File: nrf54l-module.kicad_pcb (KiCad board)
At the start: 4 copper layers, 16 x 25 mm, 127 parts, among them SW1 TS24CA, U1 NRF54L15-QFAA-R, U2 XL-0201SURC, U3 TLV62569DBVR, U4 XL-0201SURC, U5 XL-0201SURC, X1 XL7EL89CKI-111YLC-32M

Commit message: chore: refactoring
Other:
- board text removed: "RESET"
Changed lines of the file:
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@@
-		)
-	)
-	(gr_text "RESET"
-		(at 27.152888 32.092612 90)
-		(layer "B.SilkS")
-		(effects
-			(font
-				(face "Comfortaa")
-				(size 0.92 0.92)
-				(thickness 0.175)
-			)
-			(justify left bottom mirror)
-		)
-		(render_cache "RESET" 90
-			(polygon
-				(pts
-					(xy 26.966447 32.224932) (xy 26.982331 32.235467) (xy 26.992865 32.251351) (xy 26.996488 32.271532)
-					(xy 26.992868 32.291664) (xy 26.982331 32.30754) (xy 26.966447 32.318075) (xy 26.946266 32.321697)
-					(xy 26.602639 32.321697) (xy 26.602639 32.512189) (xy 26.601347 32.534098) (xy 26.970759 32.765767)
-					(xy 26.990083 32.783125) (xy 26.994729 32.793927) (xy 26.996488 32.809528) (xy 26.993573 32.831362)
-					(xy 26.985773 32.846392) (xy 26.973343 32.856491) (xy 26.957874 32.861081) (xy 26.940331 32.859188)
-					(xy 26.919246 32.849413) (xy 26.58073 32.63836) (xy 26.555079 32.694935) (xy 26.520313 32.742607)
-					(xy 26.475906 32.782507) (xy 26.424256 32.812252) (xy 26.366627 32.830315) (xy 26.30148 32.836548)
-					(xy 26.241714 32.831699) (xy 26.188233 32.81765) (xy 26.139918 32.794697) (xy 26.096596 32.763339)
-					(xy 26.060311 32.725178) (xy 26.030544 32.679537) (xy 26.009042 32.629291) (xy 25.995837 32.573848)
-					(xy 25.991277 32.512189) (xy 26.087787 32.512189) (xy 26.090935 32.55529) (xy 26.100032 32.593884)
-					(xy 26.114807 32.628698) (xy 26.135305 32.660382) (xy 26.160299 32.687047) (xy 26.190139 32.709142)
-					(xy 26.223419 32.725388) (xy 26.260268 32.735319) (xy 26.30148 32.738746) (xy 26.340041 32.735357)
-					(xy 26.374966 32.725468) (xy 26.406978 32.709142) (xy 26.435547 32.687149) (xy 26.459706 32.660499)
-					(xy 26.479726 32.628698) (xy 26.494152 32.593918) (xy 26.503048 32.555321) (xy 26.506128 32.512189)
-					(xy 26.506128 32.321697) (xy 26.087787 32.321697) (xy 26.087787 32.512189) (xy 25.991277 32.512189)
-					(xy 25.991277 32.271532) (xy 25.994899 32.251351) (xy 26.005433 32.235467) (xy 26.02131 32.22493)
-					(xy 26.041442 32.22131) (xy 26.946266 32.22131)
-				)
-			)
-			(polygon
-				(pts
-					(xy 26.996488 33.066982) (xy 26.992865 33.046801) (xy 26.982331 33.030917) (xy 26.966447 33.020383)
-					(xy 26.946266 33.01676) (xy 26.041442 33.01676) (xy 26.02131 33.02038) (xy 26.005433 33.030917)
-					(xy 25.994899 33.046801) (xy 25.991277 33.066982) (xy 25.991277 33.670591) (xy 25.994686 33.689811)
-					(xy 26.004815 33.705982) (xy 26.020191 33.717021) (xy 26.04015 33.720812) (xy 26.058054 33.717162)
-					(xy 26.073631 33.705982) (xy 26.084241 33.689764) (xy 26.087787 33.670591) (xy 26.087787 33.117147)
-					(xy 26.443043 33.117147) (xy 26.443043 33.52004) (xy 26.446663 33.540172) (xy 26.457199 33.556049)
-					(xy 26.472897 33.566642) (xy 26.491916 33.570205) (xy 26.510983 33.566639) (xy 26.526689 33.556049)
-					(xy 26.537225 33.540172) (xy 26.540845 33.52004) (xy 26.540845 33.117147) (xy 26.899977 33.117147)
-					(xy 26.899977 33.670591) (xy 26.903523 33.689764) (xy 26.914134 33.705982) (xy 26.929703 33.717164)
-					(xy 26.947558 33.720812) (xy 26.967576 33.71702) (xy 26.983005 33.705982) (xy 26.993091 33.689816)
-					(xy 26.996488 33.670591)
-				)
-			)
-			(polygon
-				(pts
-					(xy 27.009352 34.216396) (xy 27.003205 34.135423) (xy 26.985453 34.063179) (xy 26.956603 33.998209)
-					(xy 26.916523 33.940019) (xy 26.869941 33.895765) (xy 26.816275 33.863724) (xy 26.796142 33.858425)
-					(xy 26.778357 33.863106) (xy 26.763987 33.87574) (xy 26.754538 33.895913) (xy 26.752913 33.91368)
-					(xy 26.758414 33.931303) (xy 26.7696 33.946535) (xy 26.785379 33.957706) (xy 26.819936 33.980934)
-					(xy 26.850784 34.013043) (xy 26.878125 34.055508) (xy 26.89767 34.102244) (xy 26.909864 34.155468)
-					(xy 26.914134 34.216396) (xy 26.908192 34.282572) (xy 26.891423 34.337853) (xy 26.864587 34.384362)
-					(xy 26.837354 34.413084) (xy 26.80511 34.433514) (xy 26.766858 34.446177) (xy 26.721057 34.450649)
-					(xy 26.671107 34.444206) (xy 26.626562 34.425197) (xy 26.585898 34.392732) (xy 26.561977 34.362535)
-					(xy 26.54165 34.323505) (xy 26.525327 34.273808) (xy 26.513825 34.211228) (xy 26.500219 34.135924)
-					(xy 26.47972 34.072692) (xy 26.45305 34.019763) (xy 26.420516 33.975682) (xy 26.379972 33.937937)
-					(xy 26.336262 33.911777) (xy 26.288604 33.896098) (xy 26.23581 33.890744) (xy 26.18482 33.895577)
-					(xy 26.139735 33.909572) (xy 26.099359 33.932595) (xy 26.064197 33.96345) (xy 26.034438 34.001522)
-					(xy 26.009927 34.047812) (xy 25.992811 34.097656) (xy 25.982134 34.153533) (xy 25.978412 34.216396)
-					(xy 25.984122 34.286236) (xy 26.000418 34.346587) (xy 26.026668 34.399136) (xy 26.061729 34.447046)
-					(xy 26.099659 34.485774) (xy 26.140592 34.516319) (xy 26.161364 34.524935) (xy 26.180477 34.524633)
-					(xy 26.197422 34.516837) (xy 26.210082 34.502162) (xy 26.215225 34.48264) (xy 26.212666 34.462896)
-					(xy 26.203299 34.445338) (xy 26.188173 34.432617) (xy 26.146481 34.398334) (xy 26.109021 34.352173)
-					(xy 26.090812 34.316678) (xy 26.078662 34.27175) (xy 26.073631 34.215104) (xy 26.078967 34.148515)
-					(xy 26.093735 34.09487) (xy 26.116774 34.051632) (xy 26.140692 34.024695) (xy 26.168929 34.005707)
-					(xy 26.202329 33.994012) (xy 26.24227 33.989895) (xy 26.283734 33.995699) (xy 26.321484 34.013059)
-					(xy 26.356813 34.043262) (xy 26.383179 34.082207) (xy 26.406497 34.142942) (xy 26.425011 34.233136)
-					(xy 26.441429 34.314395) (xy 26.463868 34.379582) (xy 26.491378 34.431344) (xy 26.523487 34.471884)
-					(xy 26.563494 34.505617) (xy 26.608783 34.529714) (xy 26.660392 34.544565) (xy 26.719765 34.549743)
-					(xy 26.780191 34.544498) (xy 26.832233 34.529516) (xy 26.877451 34.505308) (xy 26.917063 34.472433)
-					(xy 26.949765 34.43261) (xy 26.975927 34.38498) (xy 26.994248 34.333423) (xy 27.005489 34.277474)
-				)
-			)
-			(polygon
-				(pts
-					(xy 26.996488 34.809781) (xy 26.992865 34.789601) (xy 26.982331 34.773717) (xy 26.966447 34.763182)
-					(xy 26.946266 34.75956) (xy 26.041442 34.75956) (xy 26.02131 34.76318) (xy 26.005433 34.773717)
-					(xy 25.994899 34.789601) (xy 25.991277 34.809781) (xy 25.991277 35.413391) (xy 25.994686 35.432611)
-					(xy 26.004815 35.448782) (xy 26.020191 35.45982) (xy 26.04015 35.463612) (xy 26.058054 35.459961)
-					(xy 26.073631 35.448782) (xy 26.084241 35.432564) (xy 26.087787 35.413391) (xy 26.087787 34.859946)
-					(xy 26.443043 34.859946) (xy 26.443043 35.26284) (xy 26.446663 35.282972) (xy 26.457199 35.298848)
-					(xy 26.472897 35.309441) (xy 26.491916 35.313005) (xy 26.510983 35.309439) (xy 26.526689 35.298848)
-					(xy 26.537225 35.282972) (xy 26.540845 35.26284) (xy 26.540845 34.859946) (xy 26.899977 34.859946)
-					(xy 26.899977 35.413391) (xy 26.903523 35.432564) (xy 26.914134 35.448782) (xy 26.929703 35.459964)
-					(xy 26.947558 35.463612) (xy 26.967576 35.45982) (xy 26.983005 35.448782) (xy 26.993091 35.432615)
-					(xy 26.996488 35.413391)
-				)
-			)
-			(polygon
-				(pts
-					(xy 26.996488 35.942455) (xy 26.992811 35.923368) (xy 26.981713 35.907064) (xy 26.965401 35.895969)
-					(xy 26.946266 35.89229) (xy 26.082619 35.89229) (xy 26.082619 35.587255) (xy 26.079298 35.568306)
-					(xy 26.069754 35.553774) (xy 26.055408 35.544174) (xy 26.037622 35.54091) (xy 26.018673 35.544231)
-					(xy 26.004141 35.553774) (xy 25.994598 35.568306) (xy 25.991277 35.587255) (xy 25.991277 36.299003)
-					(xy 25.994596 36.317904) (xy 26.004141 36.332428) (xy 26.018677 36.342015) (xy 26.037622 36.345348)
-					(xy 26.055404 36.342072) (xy 26.069754 36.332428) (xy 26.0793 36.317904) (xy 26.082619 36.299003)
-					(xy 26.082619 35.992676) (xy 26.946266 35.992676) (xy 26.965449 35.989132) (xy 26.981713 35.97852)
-					(xy 26.992728 35.962585)
-				)
-			)
 		)
 	)

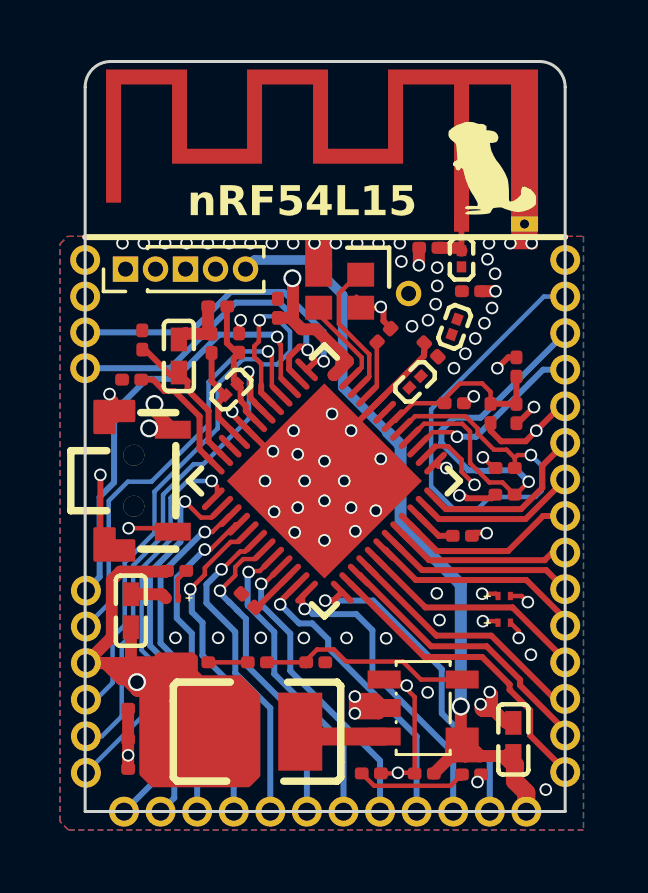
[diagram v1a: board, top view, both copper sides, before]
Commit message: feat: 1.27 mm pitch
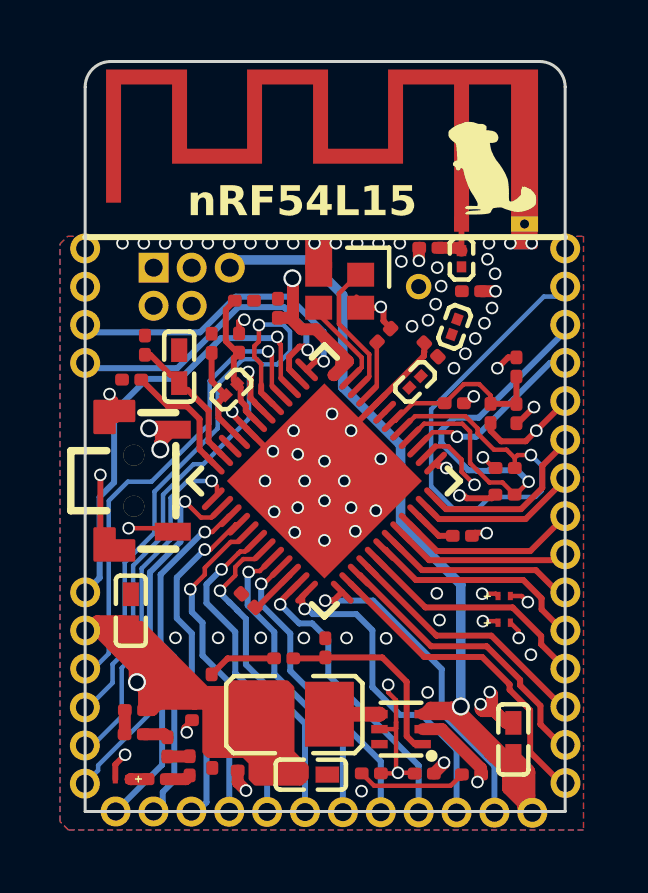
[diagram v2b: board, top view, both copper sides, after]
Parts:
- removed the ? at (25.8, 41.5)
- removed the ? at (32.0, 45.3)
- removed the ? at (25.8, 30.5)
- removed the ? at (40.5, 45.3)
- removed the ? at (39.3, 45.3)
- removed the ? at (41.8, 36.6)
- removed the ? at (25.8, 44.0)
- removed the ? at (41.8, 37.8)
- removed the ? at (41.8, 35.4)
- removed the ? at (41.8, 29.3)
- removed the ? at (41.8, 39.1)
- removed the ? at (41.8, 31.7)
- removed the ? at (30.8, 45.3)
- removed the ? at (41.8, 40.3)
- removed the ? at (41.8, 28.1)
- removed the ? at (36.9, 45.3)
- removed the ? at (41.8, 42.7)
- removed the ? at (41.8, 41.5)
- removed the ? at (25.8, 37.9)
- removed the ? at (25.8, 29.3)
- removed the ? at (35.6, 45.3)
- removed the ? at (41.8, 33.0)
- removed the ? at (38.1, 45.3)
- removed the ? at (34.4, 45.3)
- removed the ? at (28.3, 45.3)
- removed the ? at (41.8, 43.9)
- removed the ? at (41.8, 30.5)
- removed the ? at (25.8, 39.1)
- removed the ? at (33.2, 45.3)
- removed the ? at (29.5, 45.3)
- removed the ? at (25.8, 42.7)
- removed the ? at (25.8, 40.3)
- removed the ? at (41.8, 34.2)
- removed the REF** at (27.2, 27.2)
- removed U3: TLV62569DBVR, easyeda2kicad:SOT-23-5_L3.0-W1.7-P0.95-LS2.8-BR
- removed kibuzzard-68448C78: G***, kibuzzard-68448C78
- removed kibuzzard-68448FBA (x2): G***, kibuzzard-68448FBA
- removed kibuzzard-68449008: G***, kibuzzard-68449008
- removed kibuzzard-68449057: G***, kibuzzard-68449057
- removed kibuzzard-684495BB: G***, kibuzzard-684495BB
- removed kibuzzard-6844ABB3: G***, kibuzzard-6844ABB3
- removed kibuzzard-6844ABB6: G***, kibuzzard-6844ABB6
- added ?: , , F.Cu at (25.8, 41.8)
- added ?: , , F.Cu at (31.9, 45.3)
- added ?: , , F.Cu at (41.8, 27.8)
- added ?: , , F.Cu at (41.8, 34.1)
- added ?: , , F.Cu at (41.8, 32.9)
- added ?: , , F.Cu at (41.8, 29.0)
- added ?: , , F.Cu at (41.8, 35.4)
- added ?: , , F.Cu at (41.8, 41.8)
- added ?: , , F.Cu at (25.8, 40.5)
- added ?: , , F.Cu at (41.8, 36.7)
- added ?: , , F.Cu at (41.8, 31.6)
- added ?: , , F.Cu at (28.1, 28.4)
- added ?: , , F.Cu at (33.1, 45.3)
- added ?: , , F.Cu at (41.8, 39.2)
- added ?: , , F.Cu at (28.1, 45.3)
- added ?: , , F.Cu at (25.8, 29.0)
- added ?: , , F.Cu at (41.8, 40.5)
- added ?: , , F.Cu at (25.8, 44.3)
- added ?: , , F.Cu at (29.3, 45.3)
- added ?: , , F.Cu at (40.7, 45.3)
- added ?: , , F.Cu at (25.8, 43.1)
- added ?: , , F.Cu at (29.4, 28.4)
- added ?: , , F.Cu at (29.4, 27.1)
- added ?: , , F.Cu at (34.4, 45.3)
- added ?: , , F.Cu at (30.6, 45.3)
- added ?: , , F.Cu at (25.8, 39.2)
- added ?: , , F.Cu at (28.1, 27.1)
- added ?: , , F.Cu at (41.8, 30.3)
- added ?: , , F.Cu at (38.2, 45.3)
- added ?: , , F.Cu at (39.5, 45.3)
- added ?: , , F.Cu at (41.8, 44.3)
- added ?: , , F.Cu at (36.9, 45.3)
- added ?: , , F.Cu at (25.8, 30.3)
- added ?: , , F.Cu at (41.8, 43.0)
- added ?: , , F.Cu at (30.6, 27.1)
- added ?: , , F.Cu at (35.7, 45.3)
- added ?: , , F.Cu at (25.8, 38.0)
- added ?: , , F.Cu at (41.8, 38.0)
- added C22: 10uF, easyeda2kicad:C0402, F.Cu at (33.3, 44.0)
- added R11: 1kΩ, Resistor_SMD:R_0201_0603Metric, F.Cu at (29.3, 43.7)
- added R12: 1kΩ, Resistor_SMD:R_0201_0603Metric, F.Cu at (28.5, 43.1)
- added R13: 1kΩ, Resistor_SMD:R_0201_0603Metric, F.Cu at (27.4, 42.7)
- added R14: 1kΩ, Resistor_SMD:R_0201_0603Metric, F.Cu at (27.4, 41.9)
- added U6: TLV62569DRLR, easyeda2kicad:SOT-563_L1.6-W1.2-P0.50-LS1.6-BL, F.Cu at (36.3, 42.5)
- added kibuzzard-6846144B: G***, kibuzzard-6846144B, B.Cu at (28.1, 25.5)
- added kibuzzard-68461451: G***, kibuzzard-68461451, B.Cu at (29.3, 25.5)
- added kibuzzard-68461457: G***, kibuzzard-68461457, B.Cu at (30.6, 25.5)
- added kibuzzard-684616DE: G***, kibuzzard-684616DE, B.Cu at (31.2, 29.5)
- added kibuzzard-6846173A: G***, kibuzzard-6846173A, B.Cu at (30.9, 28.4)
- added kibuzzard-68461772: G***, kibuzzard-68461772, B.Cu at (29.1, 22.0)
- added kibuzzard-68461788: G***, kibuzzard-68461788, B.Cu at (34.8, 27.8)
- added kibuzzard-684617E6: G***, kibuzzard-684617E6, B.Cu at (39.9, 44.3)
- added kibuzzard-684617F6: G***, kibuzzard-684617F6, B.Cu at (27.8, 44.3)
- L4: value 2.2uH -> 1uH; footprint easyeda2kicad:IND-SMD_L3.2-W2.5-LQH32CN1R0M53L -> easyeda2kicad:L1008
- moved R2 6.97 mm to (28.2, 44.2), turned to 0 degrees
- moved U2 6.26 mm to (27.0, 44.2)
- moved kibuzzard-68448B88 6.21 mm to (28.5, 23.1)
- moved C21 3.65 mm to (31.2, 43.9)
- moved C20 2.57 mm to (30.0, 43.5), turned to -90 degrees
- moved C19 2.16 mm to (29.7, 42.2)
- moved kibuzzard-68448C52 1.41 mm to (27.8, 40.5)
- moved L4 1.37 mm to (32.8, 42.0), turned to 180 degrees
- moved kibuzzard-68448C5C 1.08 mm to (27.2, 39.2)
- moved C5 0.91 mm to (31.1, 28.2), turned to 180 degrees
- moved R4 0.89 mm to (32.4, 40.2)
- moved R3 0.84 mm to (30.0, 41.0), turned to 90 degrees
- moved R5 0.58 mm to (33.8, 39.8), turned to 90 degrees
- moved kibuzzard-68449000 0.42 mm to (27.9, 20.9)
- moved ? 0.41 mm to (36.9, 27.8)
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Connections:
- R2 pad 2: +1V8 -> Net-(R11-Pad1)
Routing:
- net +1V8: track 52.3 -> 66.8 mm
- net VIN: track 28.6 -> 38.7 mm, vias 1 -> 2
- net nRESET: track 35.5 -> 43.9 mm
- net SWDCLK: track 17.1 -> 15.0 mm
- net P1.12: track 14.4 -> 16.3 mm
- net GND: track 32.9 -> 34.3 mm
- net Net-(U6-SW): track 2.86 -> 1.67 mm
- net SW_EN: track 22.2 -> 23.3 mm
- net Net-(R3-Pad2): track 1.32 -> 2.30 mm
- net Net-(R12-Pad2): track 0.00 -> 0.83 mm
- net Net-(R11-Pad1): track 0.00 -> 0.81 mm
- net Net-(R13-Pad2): track 0.00 -> 0.81 mm
- net Net-(R11-Pad2): track 0.00 -> 0.74 mm
- net SW_FB: track 7.26 -> 6.58 mm
- net P2.01: track 10.4 -> 10.9 mm

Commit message: chore: refactoring
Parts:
- moved kibuzzard-684616DE 0.48 mm to (30.8, 29.5)
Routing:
- net GND: vias 76 -> 68

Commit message: chore: refactoring
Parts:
- removed kibuzzard-68448DC1: G***, kibuzzard-68448DC1
- removed kibuzzard-68449249: G***, kibuzzard-68449249
- added kibuzzard-684623CD: G***, kibuzzard-684623CD, B.Cu at (35.1, 39.2)
- added kibuzzard-684623E2: G***, kibuzzard-684623E2, B.Cu at (39.8, 31.6)
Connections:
- ? pad 1: nRESET -> P2.02
- ? pad 1: P2.02 -> GND
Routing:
- net P2.02: track 11.2 -> 20.2 mm
- net nRESET: track 43.9 -> 42.0 mm
- net P0.04: track 19.8 -> 19.2 mm
- net GND: track 34.3 -> 34.4 mm, vias 68 -> 70

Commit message: chore: refactoring
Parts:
- moved C17 0.96 mm to (39.3, 42.3), turned to 180 degrees
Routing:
- net VIN: track 38.6 -> 33.2 mm

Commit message: chore: refactoring
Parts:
- removed kibuzzard-68448C4F: G***, kibuzzard-68448C4F
- removed kibuzzard-68448C52: G***, kibuzzard-68448C52
- removed kibuzzard-68448C5C: G***, kibuzzard-68448C5C
- removed kibuzzard-68448C64: G***, kibuzzard-68448C64
- removed kibuzzard-68448C67: G***, kibuzzard-68448C67
- removed kibuzzard-684617F6: G***, kibuzzard-684617F6
- added kibuzzard-68463A68: G***, kibuzzard-68463A68, B.Cu at (27.7, 44.3)
- added kibuzzard-68463A73: G***, kibuzzard-68463A73, B.Cu at (27.8, 43.1)
- added kibuzzard-68463A78: G***, kibuzzard-68463A78, B.Cu at (27.8, 41.8)
- added kibuzzard-68463A7B: G***, kibuzzard-68463A7B, B.Cu at (27.8, 40.5)
- added kibuzzard-68463A81: G***, kibuzzard-68463A81, B.Cu at (27.8, 37.9)
- added kibuzzard-68463A85: G***, kibuzzard-68463A85, B.Cu at (27.2, 39.2)
- moved kibuzzard-68449000 0.54 mm to (28.5, 20.9)
- moved kibuzzard-68448B88 0.53 mm to (29.0, 23.1)
- moved kibuzzard-68461772 0.49 mm to (29.6, 22.0)
- moved kibuzzard-68449303 0.37 mm to (30.6, 43.1)
- moved kibuzzard-68449307 0.35 mm to (31.9, 43.1)
- moved kibuzzard-6844931D 0.34 mm to (36.9, 43.1)
- moved kibuzzard-6844930A 0.34 mm to (33.1, 43.1)
- moved kibuzzard-68449316 0.34 mm to (35.7, 43.1)
- moved kibuzzard-6844930F 0.33 mm to (34.4, 43.1)
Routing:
- net P0.03: track 15.2 -> 12.8 mm
- net nRESET: track 42.0 -> 40.7 mm
- net SW_EN: track 22.9 -> 24.2 mm
- net P1.00: track 13.3 -> 14.0 mm
- net Net-(R10-Pad1): track 3.61 -> 4.23 mm
